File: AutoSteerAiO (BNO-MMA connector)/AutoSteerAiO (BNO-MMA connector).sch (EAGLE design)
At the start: 87 parts, among them J4 CONNECTOR 1x5 PINS, K4 CB1A-P-12V, T1 BC547, U1 VX7805-1000

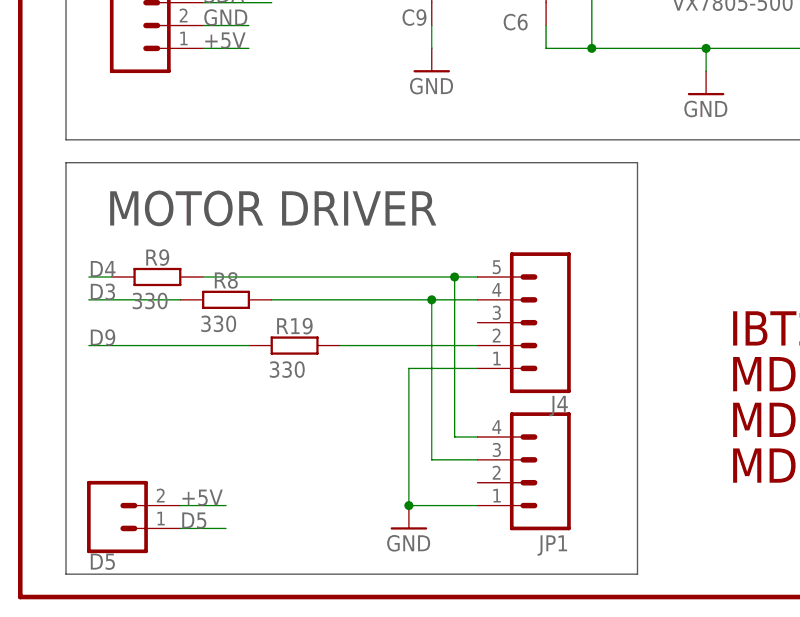
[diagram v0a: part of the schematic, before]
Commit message: Add files via upload
One connector for all motor drivers
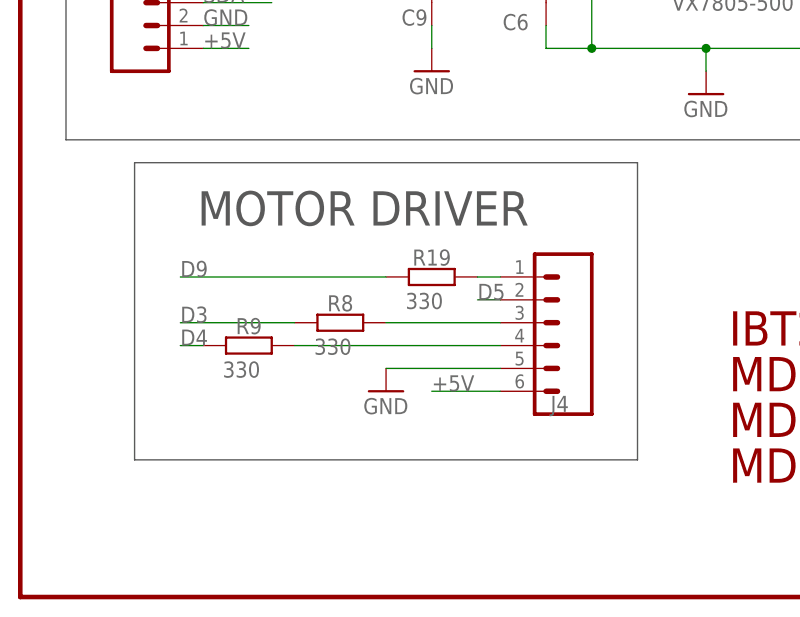
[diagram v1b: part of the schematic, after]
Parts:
- removed D5: CONNECTOR 1x1 PIN, SparkFun-Connectors:CONN_02
- removed JP1: CONNECTOR 1x4 PINS, Header and Connector:2600-04_(NORMAL)
- J4: device Header and Connector:2600-05_(NORMAL) -> SparkFun-Connectors:CONN_06SILK_FEMALE_PTH
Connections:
- net +5V: now also J4.6; no longer D5.2
- net D5: now also J4.2; no longer D5.1
- net GND: now also J4.5; no longer J4.1, JP1.1
- net N$19: now also J4.4; no longer J4.5, JP1.4
- net N$20: now also J4.3; no longer J4.4, JP1.3
- net N$22: now also J4.1; no longer J4.2
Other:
- moved on the sheet: R19, R8, R9

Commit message: Add files via upload
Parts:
- removed 15V1, 15V2, GND, GND30: WIREPAD4,16O1,6, wirepad:WIREPAD4,16O1,6
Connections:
- net +15V: no longer 15V1.P, 15V2.P
- net GND: no longer GND.P, GND30.P
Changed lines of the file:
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@@
 <attribute name="OC_NEWARK" value="unknown"/>
 </part>
-<part name="15V1" library="wirepad" library_urn="urn:adsk.eagle:library:412" deviceset="WIREPAD" device="4,16O1,6" package3d_urn="urn:adsk.eagle:package:30843/1">
-<attribute name="MF" value=""/>
-<attribute name="MPN" value=""/>
-<attribute name="OC_NEWARK" value="unknown"/>
-</part>
-<part name="15V2" library="wirepad" library_urn="urn:adsk.eagle:library:412" deviceset="WIREPAD" device="4,16O1,6" package3d_urn="urn:adsk.eagle:package:30843/1">
-<attribute name="MF" value=""/>
-<attribute name="MPN" value=""/>
-<attribute name="OC_NEWARK" value="unknown"/>
-</part>
-<part name="GND" library="wirepad" library_urn="urn:adsk.eagle:library:412" deviceset="WIREPAD" device="4,16O1,6" package3d_urn="urn:adsk.eagle:package:30843/1">
-<attribute name="MF" value=""/>
-<attribute name="MPN" value=""/>
-<attribute name="OC_NEWARK" value="unknown"/>
-</part>
-<part name="GND30" library="wirepad" library_urn="urn:adsk.eagle:library:412" deviceset="WIREPAD" device="4,16O1,6" package3d_urn="urn:adsk.eagle:package:30843/1">
-<attribute name="MF" value=""/>
-<attribute name="MPN" value=""/>
-<attribute name="OC_NEWARK" value="unknown"/>
-</part>
-<part name="GND22" library="supply1" library_urn="urn:adsk.eagle:library:371" deviceset="GND" device=""/>
 <part name="J4" library="SparkFun-Connectors" library_urn="urn:adsk.eagle:library:513" deviceset="CONN_06" device="SILK_FEMALE_PTH" package3d_urn="urn:adsk.eagle:package:38009/1" value="CONNECTOR 1x5 PINS">
 <attribute name="MF" value=""/>
@@
 <attribute name="MPN" x="10.16" y="240.03" size="1.778" layer="96" display="off"/>
 </instance>
-<instance part="15V1" gate="G$1" x="53.34" y="275.59" smashed="yes" rot="R270">
-<attribute name="NAME" x="55.1942" y="276.733" size="1.778" layer="95" rot="R270"/>
-<attribute name="OC_NEWARK" x="53.34" y="275.59" size="1.778" layer="96" display="off"/>
-<attribute name="MF" x="53.34" y="275.59" size="1.778" layer="96" display="off"/>
-<attribute name="MPN" x="53.34" y="275.59" size="1.778" layer="96" display="off"/>
-</instance>
-<instance part="15V2" gate="G$1" x="58.42" y="275.59" smashed="yes" rot="R270">
-<attribute name="NAME" x="60.2742" y="276.733" size="1.778" layer="95" rot="R270"/>
-<attribute name="OC_NEWARK" x="58.42" y="275.59" size="1.778" layer="96" display="off"/>
-<attribute name="MF" x="58.42" y="275.59" size="1.778" layer="96" display="off"/>
-<attribute name="MPN" x="58.42" y="275.59" size="1.778" layer="96" display="off"/>
-</instance>
-<instance part="GND" gate="G$1" x="66.04" y="275.59" smashed="yes" rot="R270">
-<attribute name="NAME" x="67.8942" y="276.733" size="1.778" layer="95" rot="R270"/>
-<attribute name="OC_NEWARK" x="66.04" y="275.59" size="1.778" layer="96" display="off"/>
-<attribute name="MF" x="66.04" y="275.59" size="1.778" layer="96" display="off"/>
-<attribute name="MPN" x="66.04" y="275.59" size="1.778" layer="96" display="off"/>
-</instance>
-<instance part="GND30" gate="G$1" x="71.12" y="275.59" smashed="yes" rot="R270">
-<attribute name="NAME" x="72.9742" y="276.733" size="1.778" layer="95" rot="R270"/>
-<attribute name="OC_NEWARK" x="71.12" y="275.59" size="1.778" layer="96" display="off"/>
-<attribute name="MF" x="71.12" y="275.59" size="1.778" layer="96" display="off"/>
-<attribute name="MPN" x="71.12" y="275.59" size="1.778" layer="96" display="off"/>
-</instance>
-<instance part="GND22" gate="1" x="71.12" y="254" smashed="yes">
-<attribute name="VALUE" x="68.58" y="251.46" size="1.778" layer="96"/>
-</instance>
 <instance part="J4" gate="G$1" x="58.42" y="93.98" smashed="yes" rot="R180">
 <attribute name="NAME" x="60.96" y="85.852" size="1.778" layer="95" font="vector" rot="R180"/>
@@
 <pinref part="C4" gate="G$1" pin="-"/>
 <pinref part="GND21" gate="1" pin="GND"/>
-</segment>
-<segment>
-<pinref part="GND22" gate="1" pin="GND"/>
-<wire x1="66.04" y1="269.24" x2="71.12" y2="269.24" width="0.1524" layer="91"/>
-<pinref part="GND30" gate="G$1" pin="P"/>
-<wire x1="71.12" y1="273.05" x2="71.12" y2="269.24" width="0.1524" layer="91"/>
-<junction x="71.12" y="269.24"/>
-<pinref part="GND" gate="G$1" pin="P"/>
-<wire x1="66.04" y1="273.05" x2="66.04" y2="269.24" width="0.1524" layer="91"/>
-<wire x1="71.12" y1="269.24" x2="71.12" y2="256.54" width="0.1524" layer="91"/>
 </segment>
 <segment>
@@
 <pinref part="P+1" gate="1" pin="+15V"/>
 <pinref part="C4" gate="G$1" pin="+"/>
-<junction x="48.26" y="269.24"/>
-<wire x1="48.26" y1="269.24" x2="48.26" y2="271.78" width="0.1524" layer="91"/>
-<pinref part="15V1" gate="G$1" pin="P"/>
-<wire x1="53.34" y1="273.05" x2="53.34" y2="269.24" width="0.1524" layer="91"/>
-<pinref part="15V2" gate="G$1" pin="P"/>
-<wire x1="53.34" y1="269.24" x2="58.42" y2="269.24" width="0.1524" layer="91"/>
-<wire x1="58.42" y1="269.24" x2="58.42" y2="273.05" width="0.1524" layer="91"/>
-<wire x1="53.34" y1="269.24" x2="48.26" y2="269.24" width="0.1524" layer="91"/>
-<junction x="53.34" y="269.24"/>
-<junction x="48.26" y="269.24"/>
 <pinref part="D2" gate="1" pin="A"/>
 <pinref part="K4" gate="2" pin="P"/>
@@
 <wire x1="43.18" y1="269.24" x2="43.18" y2="266.7" width="0.1524" layer="91"/>
 <wire x1="43.18" y1="266.7" x2="43.18" y2="243.84" width="0.1524" layer="91"/>
-<wire x1="48.26" y1="269.24" x2="48.26" y2="266.7" width="0.1524" layer="91"/>
+<wire x1="48.26" y1="271.78" x2="48.26" y2="266.7" width="0.1524" layer="91"/>
 <wire x1="43.18" y1="266.7" x2="48.26" y2="266.7" width="0.1524" layer="91"/>
 <junction x="43.18" y="266.7"/>

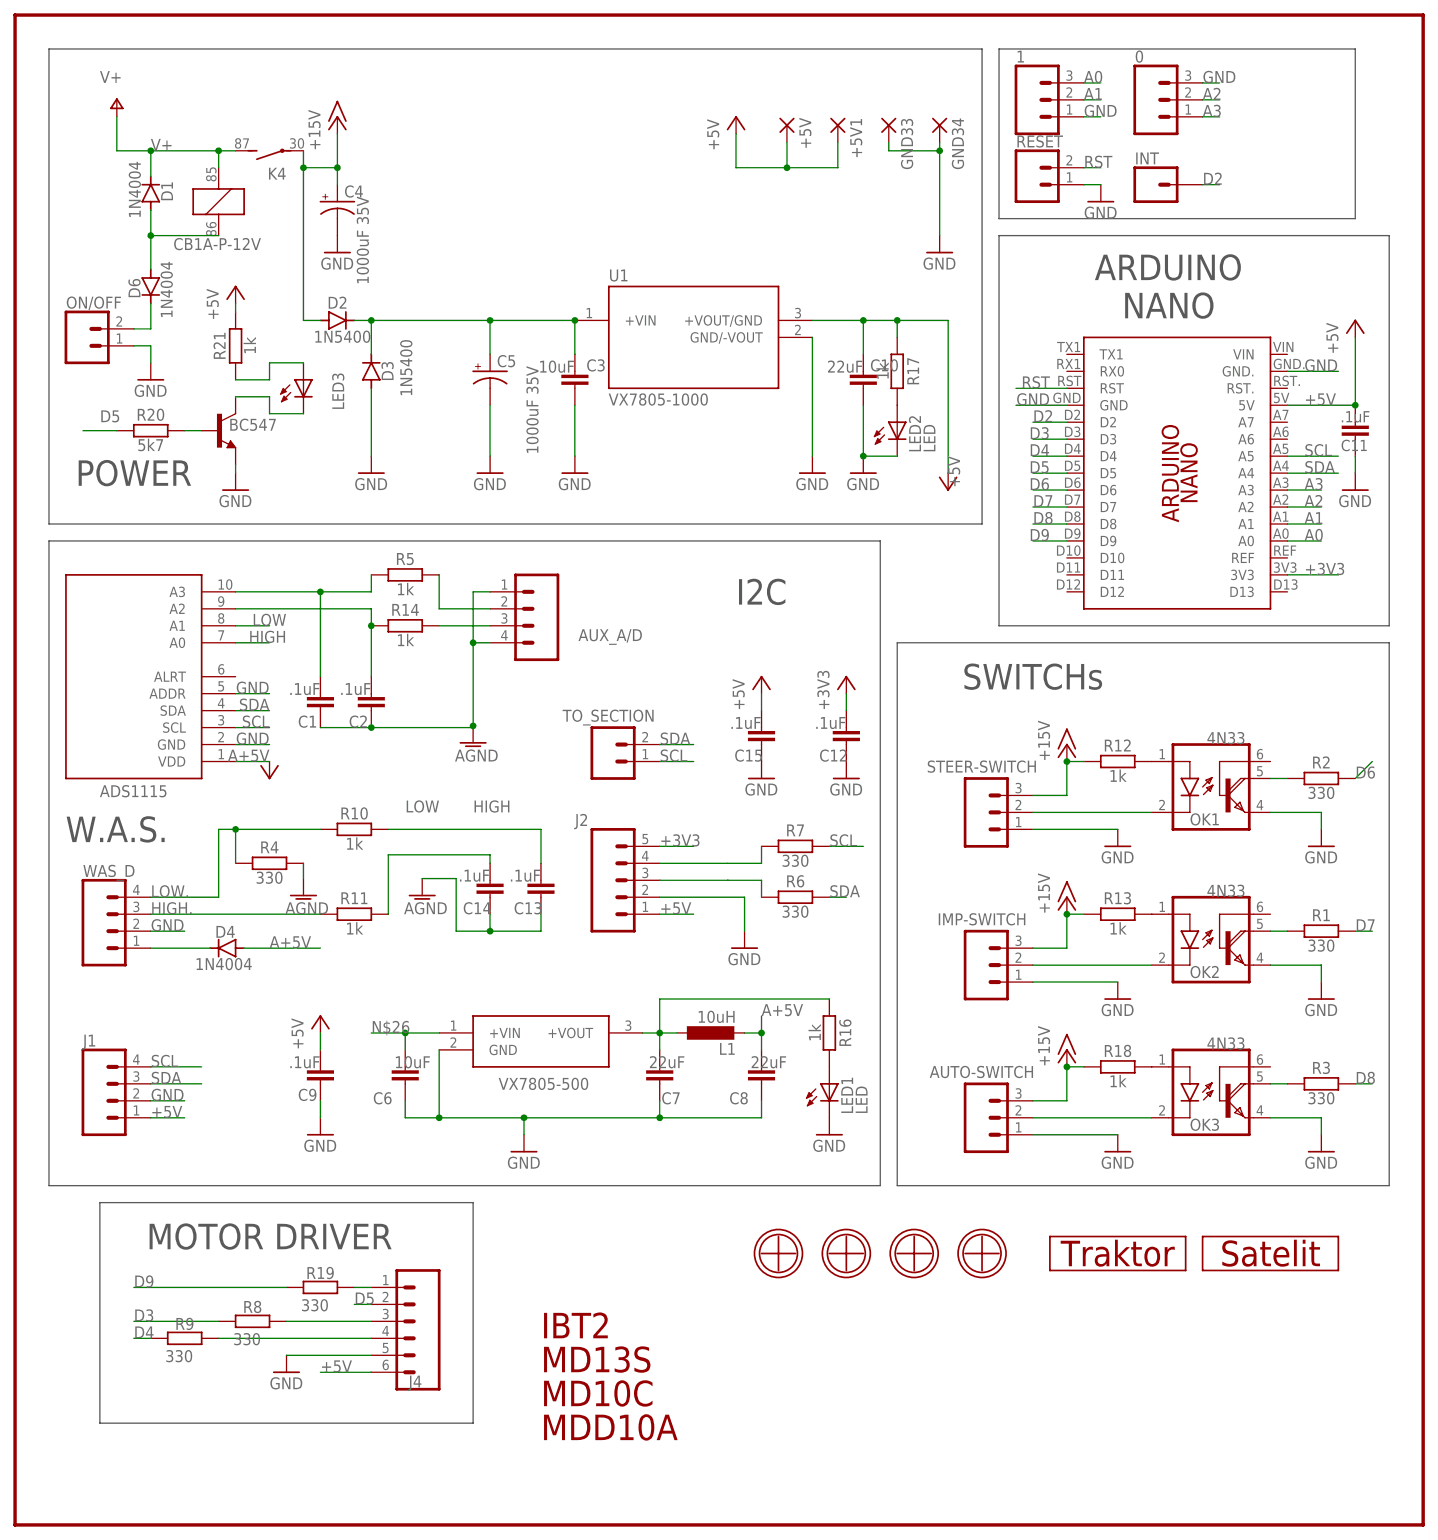
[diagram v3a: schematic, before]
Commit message: Add files via upload
Added connector for SWEncoder
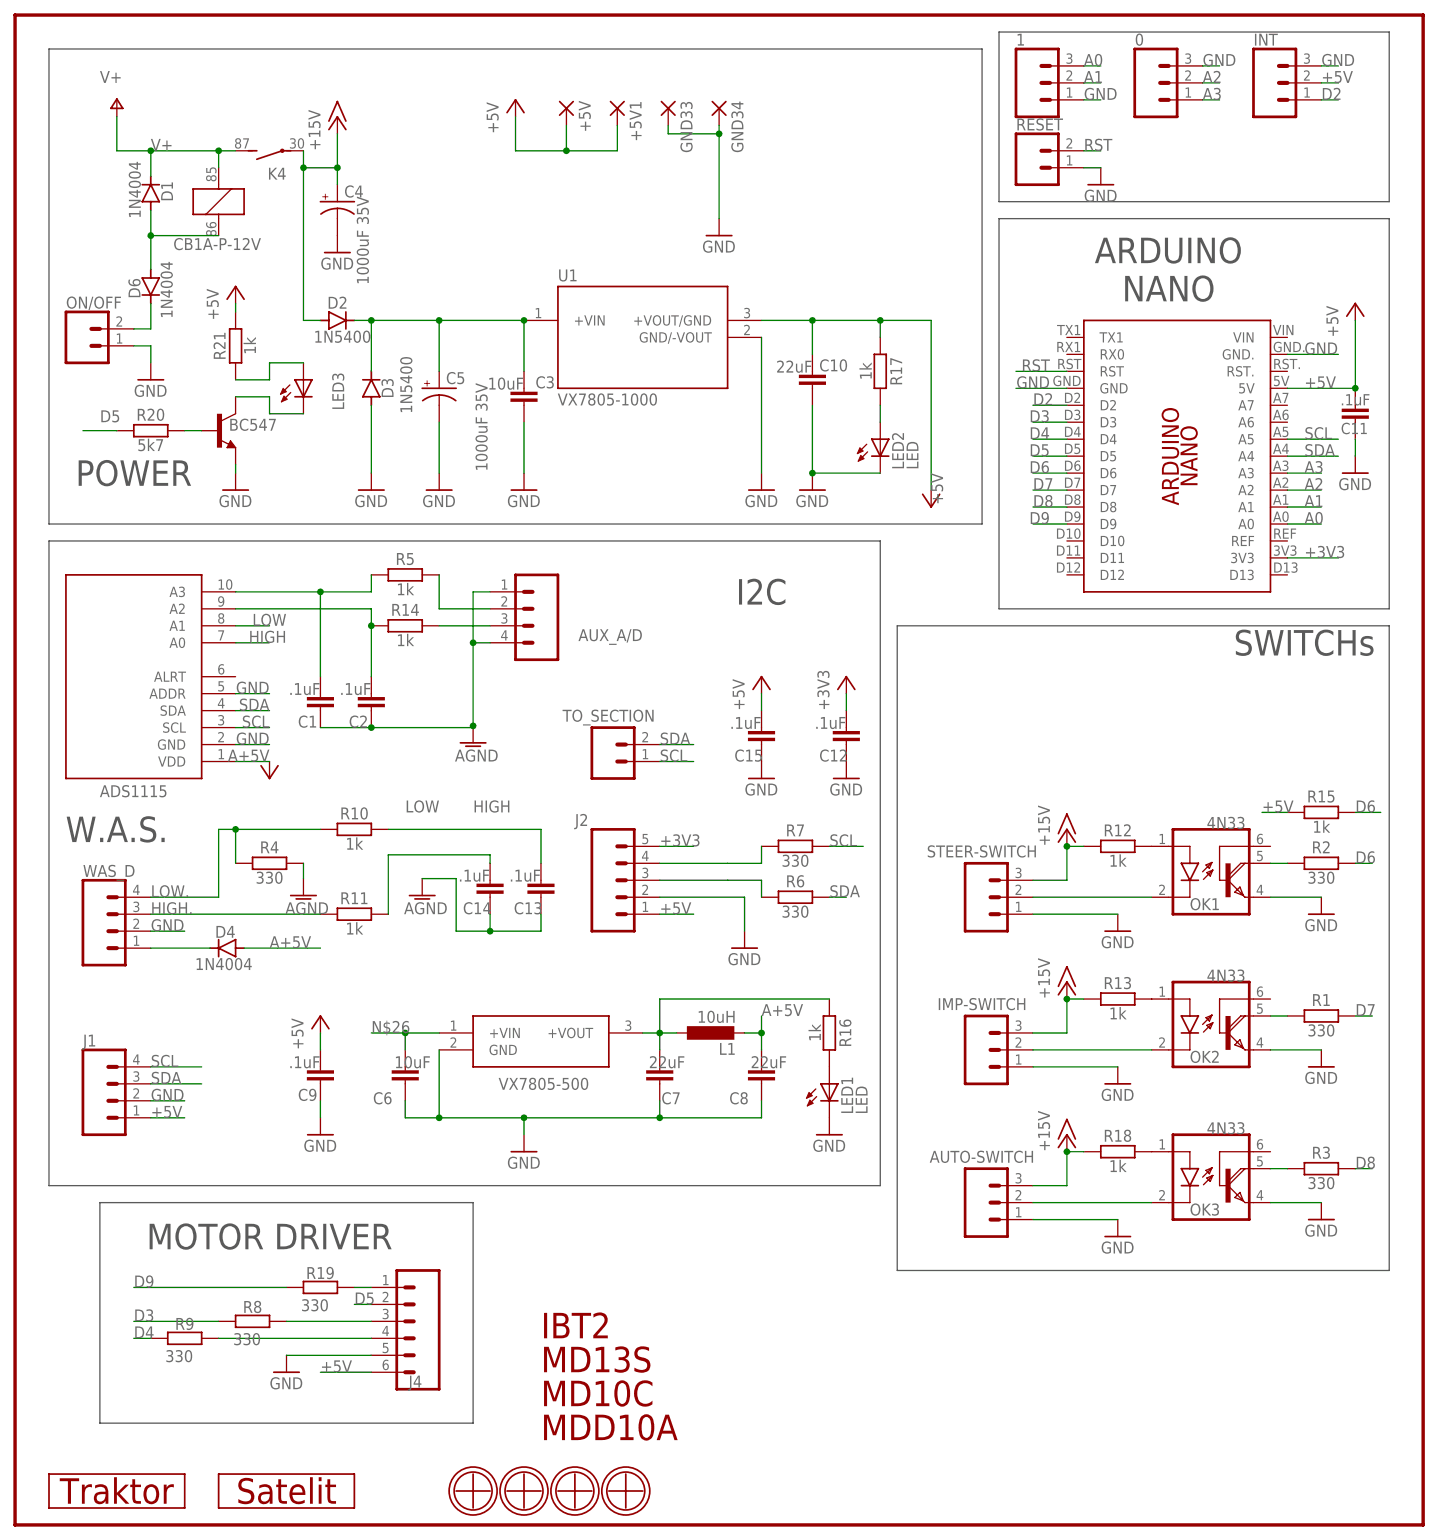
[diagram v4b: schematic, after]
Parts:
- added R15: 1k, resistor:R-EU_0207/7
- INT: value CONNECTOR 1x1 PIN -> (none); device SparkFun-Connectors:CONN_01 -> SparkFun-Connectors:CONN_03; OC_NEWARK unknown -> (none)
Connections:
- net +5V: now also INT.2, R15.1
- net D6: now also R15.2
- net GND: now also INT.3
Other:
- moved on the sheet: +5V, +5V1, 0, 1, AUTO-SWITCH, C10, C11, C3, C5, D3, GND33, GND34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

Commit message: Add files via upload
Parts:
- removed +5V, +5V1, GND33, GND34: (no value), wirepad:2,15/1,0
- removed INT: (no value), SparkFun-Connectors:CONN_03
- added 5V: CONNECTOR 1x2 PINS, SparkFun-Connectors:CONN_02
- added D5: 1N4004, diode:1N4004
- added ENCODER: CONNECTOR 1x3 PINS, SparkFun-Connectors:CONN_04
- added OK4: 4N33, #optocoupler:4N33
- added R22: 330, resistor:R-EU_0207/7
- added R23: 1k, resistor:R-EU_0207/7
- LED1, LED2, LED3: device adafruit:LED5MM -> led:LED3MM
- OK1, OK2, OK3: device optocoupler:4N33 -> #optocoupler:4N33
- renumbered AUTO-SWITCH to REMOTE-SWITCH
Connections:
- new net N$29: OK4.COL, R22.1
- new net N$30: OK4.A, R23.2
- new net N$31: ENCODER.3, OK4.C
- new net N$32: D5.C, ENCODER.4
- net +15V: now also ENCODER.1, R23.1
- net +5V: now also 5V.2, D5.A; no longer +5V.P, +5V1.P, INT.2
- net D2: now also R22.2; no longer INT.1
- net GND: now also 5V.1, ENCODER.2, OK4.E; no longer GND33.P, GND34.P, INT.3
- net RST: now also PCB1.RST.; no longer PCB1.RST

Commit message: Add files via upload
Added connector for ibt2 driver for connection with Flat ribbon cable
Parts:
- removed J4: CONNECTOR 1x5 PINS, SparkFun-Connectors:CONN_06SILK_FEMALE_PTH
- added IBT2: (no value), SparkFun-Connectors:CONN_04X2
- added J3: (no value), SparkFun-Connectors:CONN_03
- added R24: 1k, resistor:R-EU_0207/7
- J1, J2, T1: OC_NEWARK (none) -> unknown
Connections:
- removed net N$19: J4.4, R9.1
- removed net N$20: J4.3, R8.1
- removed net N$22: J4.1, R19.1
- new net DIR: J3.1, R9.1
- new net PWM1: IBT2.2, J3.2, R8.1
- new net PWM2: IBT2.1, R19.1
- net +5V: now also IBT2.7, R24.1; no longer J4.6
- net D2: now also R24.2
- net D5: now also IBT2.3, IBT2.4; no longer J4.2
- net GND: now also IBT2.8, J3.3; no longer J4.5
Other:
- moved on the sheet: R19, R8, R9
